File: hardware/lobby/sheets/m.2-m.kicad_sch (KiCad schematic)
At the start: 1 part

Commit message: start routing mezzanine
making a progress capture before trying to cram a lot of signals onto just one hirose connector...
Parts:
- U2: renamed from U?; footprint CM4IO:M.2 - M - MDT420M01002 -> cm4crypto:M.2 - M - MDT420M01002
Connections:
- no-connect marks 0 -> 20
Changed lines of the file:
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@@
   (junction (at 166.37 138.43) (diameter 1.016) (color 0 0 0 0))
   (junction (at 166.37 140.97) (diameter 1.016) (color 0 0 0 0))
+  (no_connect (at 132.08 57.15))
+  (no_connect (at 132.08 59.69))
+  (no_connect (at 132.08 64.77))
+  (no_connect (at 132.08 67.31))
+  (no_connect (at 132.08 72.39))
+  (no_connect (at 132.08 74.93))
+  (no_connect (at 132.08 80.01))
+  (no_connect (at 132.08 82.55))
+  (no_connect (at 132.08 87.63))
+  (no_connect (at 132.08 90.17))
+  (no_connect (at 132.08 95.25))
+  (no_connect (at 132.08 97.79))
+  (no_connect (at 132.08 138.43))
+  (no_connect (at 165.1 62.23))
+  (no_connect (at 165.1 97.79))
+  (no_connect (at 165.1 100.33))
+  (no_connect (at 165.1 102.87))
+  (no_connect (at 165.1 105.41))
+  (no_connect (at 165.1 118.11))
+  (no_connect (at 165.1 135.89))
   (wire (pts (xy 130.81 52.07) (xy 132.08 52.07))
     (stroke (width 0) (type solid) (color 0 0 0 0))
@@
   (symbol (lib_id "power:GND") (at 130.81 151.13 0) (unit 1)
     (in_bom yes) (on_board yes)
-    (property "Reference" "#PWR?" (id 0) (at 130.81 157.48 0)
+    (property "Reference" "#PWR060" (id 0) (at 130.81 157.48 0)
       (effects (font (size 1.27 1.27)) hide)
     )
@@
   (symbol (lib_id "CM4IO:M.2-keyM") (at 152.4 46.99 0) (unit 1)
     (in_bom yes) (on_board yes) (fields_autoplaced)
-    (property "Reference" "U?" (id 0) (at 135.89 48.26 0)
+    (property "Reference" "U2" (id 0) (at 135.89 48.26 0)
       (effects (font (size 1.27 1.27)) hide)
     )
     (property "Value" "M.2-keyM" (id 1) (at 148.59 49.53 0))
-    (property "Footprint" "CM4IO:M.2 - M - MDT420M01002" (id 2) (at 148.59 151.13 0)
-      (effects (font (size 1.27 1.27)) hide)
-    )
+    (property "Footprint" "cm4crypto:M.2 - M - MDT420M01002" (id 2) (at 148.59 151.13 0)
+      (effects (font (size 1.27 1.27)) hide)
+    )

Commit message: sheet refs relative, copied escalator pinout to lobby
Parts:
- renumbered U2 to U?
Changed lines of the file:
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@@
   (symbol (lib_id "power:GND") (at 130.81 151.13 0) (unit 1)
     (in_bom yes) (on_board yes)
-    (property "Reference" "#PWR060" (id 0) (at 130.81 157.48 0)
+    (property "Reference" "#PWR?" (id 0) (at 130.81 157.48 0)
       (effects (font (size 1.27 1.27)) hide)
     )
@@
   (symbol (lib_id "CM4IO:M.2-keyM") (at 152.4 46.99 0) (unit 1)
     (in_bom yes) (on_board yes) (fields_autoplaced)
-    (property "Reference" "U2" (id 0) (at 135.89 48.26 0)
+    (property "Reference" "U?" (id 0) (at 135.89 48.26 0)
       (effects (font (size 1.27 1.27)) hide)
     )

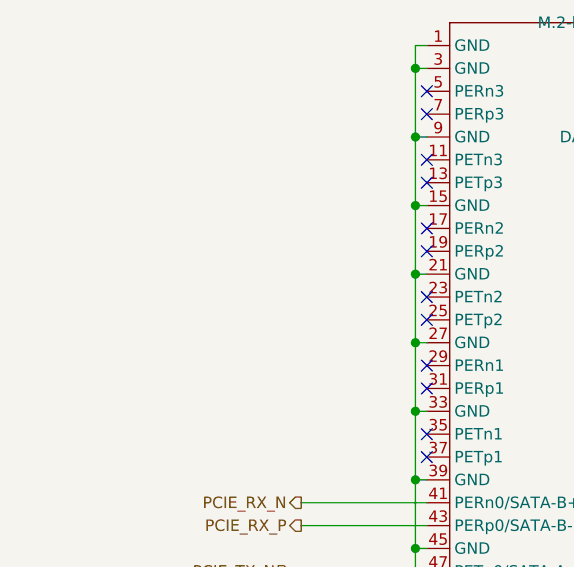
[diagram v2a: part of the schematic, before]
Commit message: work abroad
did some light planning for the lobby board while on vacation. now ready for final placement + routing
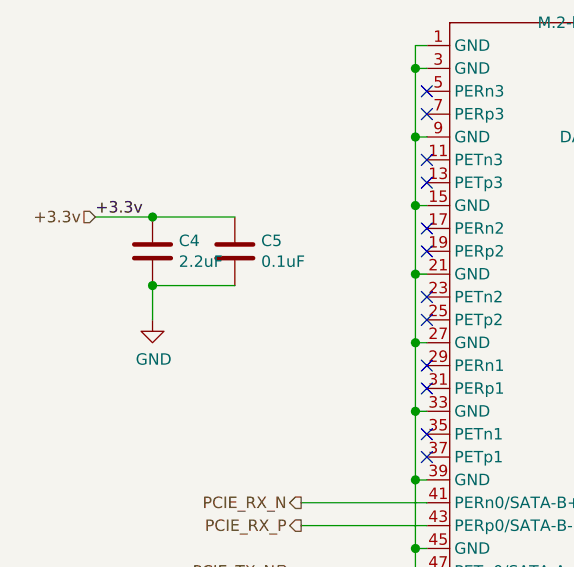
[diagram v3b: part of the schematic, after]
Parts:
- added C4: 2.2uF, Capacitor_SMD:C_0603_1608Metric, symbol Device:C
- added C5: 0.1uF, Capacitor_SMD:C_0603_1608Metric, symbol Device:C
- gave numbers to parts that had none: 1
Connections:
- net +3.3v: now also C4.1, C5.1
- net GND: now also C4.2, C5.2
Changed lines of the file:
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@@
 (kicad_sch (version 20210406) (generator eeschema)
   (paper "A4")
+  (junction (at 101.6 71.12) (diameter 1.016) (color 0 0 0 0))
+  (junction (at 101.6 78.74) (diameter 1.016) (color 0 0 0 0))
   (junction (at 130.81 54.61) (diameter 1.016) (color 0 0 0 0))
   (junction (at 130.81 62.23) (diameter 1.016) (color 0 0 0 0))
@@
   (no_connect (at 165.1 118.11))
   (no_connect (at 165.1 135.89))
+  (wire (pts (xy 95.25 71.12) (xy 101.6 71.12))
+    (stroke (width 0) (type solid) (color 0 0 0 0))
+  )
+  (wire (pts (xy 101.6 71.12) (xy 110.744 71.12))
+    (stroke (width 0) (type solid) (color 0 0 0 0))
+  )
+  (wire (pts (xy 101.6 78.74) (xy 110.744 78.74))
+    (stroke (width 0) (type solid) (color 0 0 0 0))
+  )
+  (wire (pts (xy 101.6 82.55) (xy 101.6 78.74))
+    (stroke (width 0) (type solid) (color 0 0 0 0))
+  )
   (wire (pts (xy 130.81 52.07) (xy 132.08 52.07))
     (stroke (width 0) (type solid) (color 0 0 0 0))
@@
     (effects (font (size 1.27 1.27)) (justify right bottom))
   )
+  (label "+3.3v" (at 95.25 71.12 0)
+    (effects (font (size 1.27 1.27)) (justify left bottom))
+  )
   (label "+3.3v" (at 142.24 29.21 0)
     (effects (font (size 1.27 1.27)) (justify left bottom))
@@
     (effects (font (size 1.27 1.27)) (justify right bottom))
   )
+  (hierarchical_label "+3.3v" (shape input) (at 95.25 71.12 180)
+    (effects (font (size 1.27 1.27)) (justify right))
+  )
   (hierarchical_label "PCIE_TX_N" (shape input) (at 116.84 110.49 180)
     (effects (font (size 1.27 1.27)) (justify right))
@@
     (effects (font (size 1.27 1.27)) (justify left))
   )
+  (symbol (lib_id "power:GND") (at 101.6 82.55 0) (unit 1)
+    (in_bom yes) (on_board yes)
+    (property "Reference" "#PWR063" (id 0) (at 101.6 88.9 0)
+      (effects (font (size 1.27 1.27)) hide)
+    )
+    (property "Value" "GND" (id 1) (at 101.727 86.9442 0))
+    (property "Footprint" "" (id 2) (at 101.6 82.55 0)
+      (effects (font (size 1.27 1.27)) hide)
+    )
+    (property "Datasheet" "" (id 3) (at 101.6 82.55 0)
+      (effects (font (size 1.27 1.27)) hide)
+    )
+    (pin "1")
+  )
   (symbol (lib_id "power:GND") (at 130.81 151.13 0) (unit 1)
     (in_bom yes) (on_board yes)
-    (property "Reference" "#PWR?" (id 0) (at 130.81 157.48 0)
+    (property "Reference" "#PWR064" (id 0) (at 130.81 157.48 0)
       (effects (font (size 1.27 1.27)) hide)
     )
@@
     (pin "1")
   )
+  (symbol (lib_id "Device:C") (at 101.6 74.93 0) (unit 1)
+    (in_bom yes) (on_board yes)
+    (property "Reference" "C4" (id 0) (at 104.521 73.7616 0)
+      (effects (font (size 1.27 1.27)) (justify left))
+    )
+    (property "Value" "2.2uF" (id 1) (at 104.521 76.073 0)
+      (effects (font (size 1.27 1.27)) (justify left))
+    )
+    (property "Footprint" "Capacitor_SMD:C_0603_1608Metric" (id 2) (at 102.5652 78.74 0)
+      (effects (font (size 1.27 1.27)) hide)
+    )
+    (property "Datasheet" "https://search.murata.co.jp/Ceramy/image/img/A01X/G101/ENG/GRM21BR71A106KA73-01.pdf" (id 3) (at 101.6 74.93 0)
+      (effects (font (size 1.27 1.27)) hide)
+    )
+    (property "Field5" "490-14381-1-ND" (id 4) (at 101.6 74.93 0)
+      (effects (font (size 1.27 1.27)) hide)
+    )
+    (property "Field4" "Digikey" (id 5) (at 101.6 74.93 0)
+      (effects (font (size 1.27 1.27)) hide)
+    )
+    (property "Field6" "GRM21BR71A106KA73L" (id 6) (at 101.6 74.93 0)
+      (effects (font (size 1.27 1.27)) hide)
+    )
+    (property "Field7" "Murata" (id 7) (at 101.6 74.93 0)
+      (effects (font (size 1.27 1.27)) hide)
+    )
+    (property "Part Description" "	10uF 10% 10V Ceramic Capacitor X7R 0805 (2012 Metric)" (id 8) (at 101.6 74.93 0)
+      (effects (font (size 1.27 1.27)) hide)
+    )
+    (property "Field8" "111893011" (id 9) (at 101.6 74.93 0)
+      (effects (font (size 1.27 1.27)) hide)
+    )
+    (pin "1")
+    (pin "2")
+  )
+  (symbol (lib_id "Device:C") (at 110.744 74.93 0) (unit 1)
+    (in_bom yes) (on_board yes)
+    (property "Reference" "C5" (id 0) (at 113.665 73.7616 0)
+      (effects (font (size 1.27 1.27)) (justify left))
+    )
+    (property "Value" "0.1uF" (id 1) (at 113.665 76.073 0)
+      (effects (font (size 1.27 1.27)) (justify left))
+    )
+    (property "Footprint" "Capacitor_SMD:C_0603_1608Metric" (id 2) (at 111.7092 78.74 0)
+      (effects (font (size 1.27 1.27)) hide)
+    )
+    (property "Datasheet" "https://search.murata.co.jp/Ceramy/image/img/A01X/G101/ENG/GRM21BR71A106KA73-01.pdf" (id 3) (at 110.744 74.93 0)
+      (effects (font (size 1.27 1.27)) hide)
+    )
+    (property "Field5" "490-14381-1-ND" (id 4) (at 110.744 74.93 0)
+      (effects (font (size 1.27 1.27)) hide)
+    )
+    (property "Field4" "Digikey" (id 5) (at 110.744 74.93 0)
+      (effects (font (size 1.27 1.27)) hide)
+    )
+    (property "Field6" "GRM21BR71A106KA73L" (id 6) (at 110.744 74.93 0)
+      (effects (font (size 1.27 1.27)) hide)
+    )
+    (property "Field7" "Murata" (id 7) (at 110.744 74.93 0)
+      (effects (font (size 1.27 1.27)) hide)
+    )
+    (property "Part Description" "	10uF 10% 10V Ceramic Capacitor X7R 0805 (2012 Metric)" (id 8) (at 110.744 74.93 0)
+      (effects (font (size 1.27 1.27)) hide)
+    )
+    (property "Field8" "111893011" (id 9) (at 110.744 74.93 0)
+      (effects (font (size 1.27 1.27)) hide)
+    )
+    (pin "1")
+    (pin "2")
+  )
   (symbol (lib_id "CM4IO:M.2-keyM") (at 152.4 46.99 0) (unit 1)
     (in_bom yes) (on_board yes) (fields_autoplaced)
-    (property "Reference" "U?" (id 0) (at 135.89 48.26 0)
-      (effects (font (size 1.27 1.27)) hide)
-    )
+    (property "Reference" "U2" (id 0) (at 135.89 48.26 0)
+      (effects (font (size 1.27 1.27)) hide)
+    )

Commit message: update m.2 connector footprint
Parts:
- U2: footprint cm4crypto:M.2 - M - MDT420M01002 -> cm4crypto:M.2 - M - Amphenol - 10131758-001RLF
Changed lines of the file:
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@@
     )
     (property "Value" "M.2-keyM" (id 1) (at 148.59 49.53 0))
-    (property "Footprint" "cm4crypto:M.2 - M - MDT420M01002" (id 2) (at 148.59 151.13 0)
+    (property "Footprint" "cm4crypto:M.2 - M - Amphenol - 10131758-001RLF" (id 2) (at 148.59 151.13 0)
       (effects (font (size 1.27 1.27)) hide)
     )
